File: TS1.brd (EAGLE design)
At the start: 32 x 22 mm, 20 parts, among them IC1 AT42QT1010, J1 PWR, Q1 2N7002

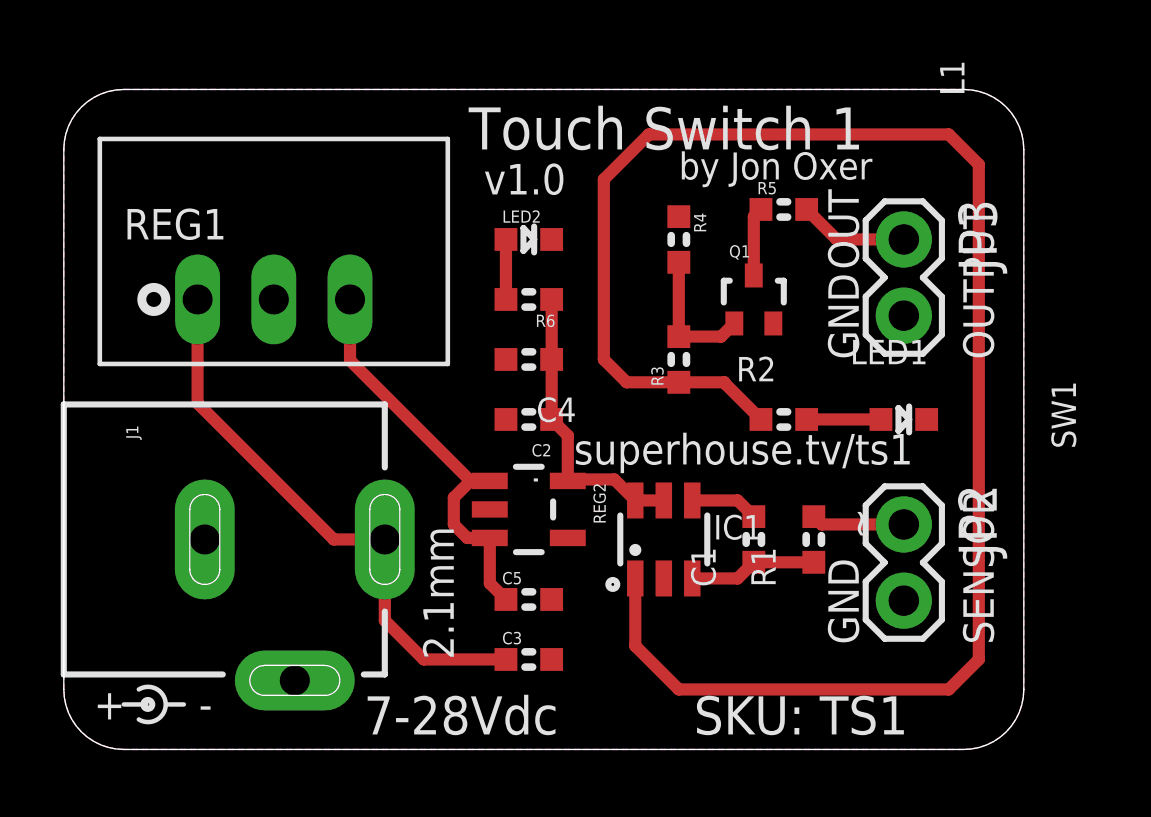
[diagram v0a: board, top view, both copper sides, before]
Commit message: Added mounting hole
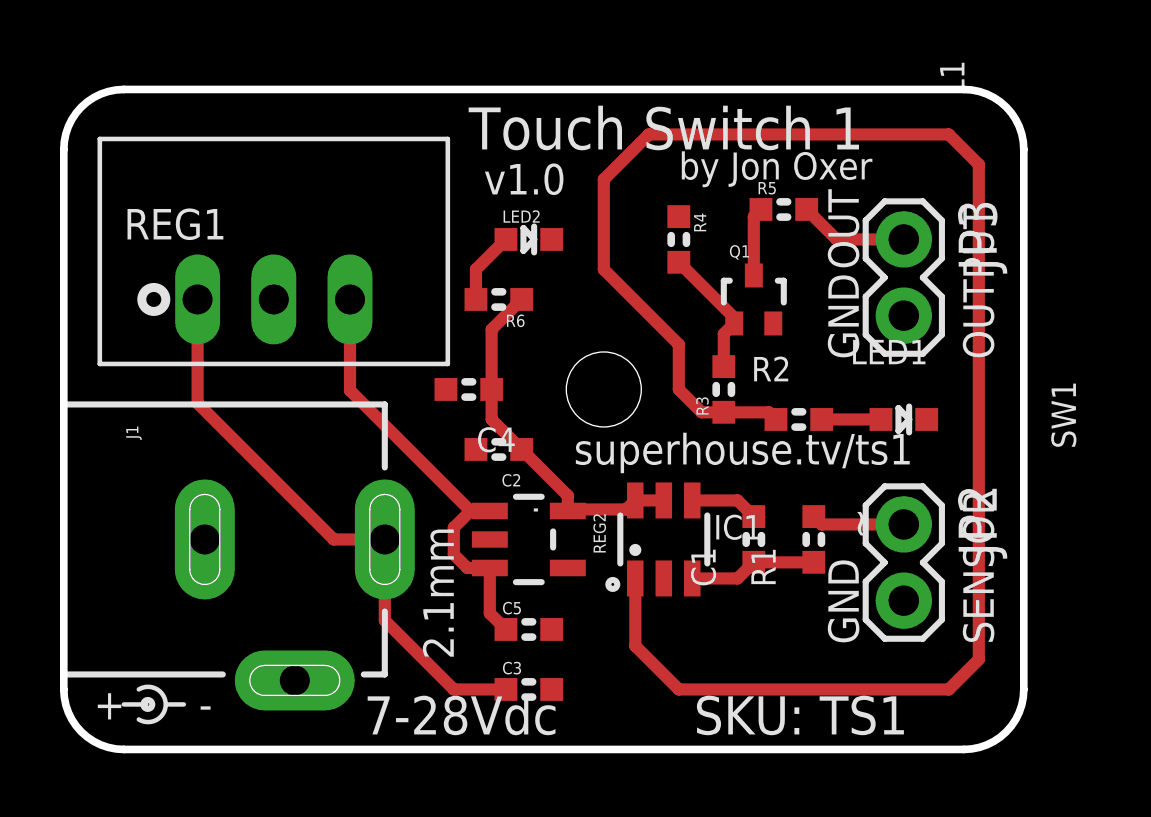
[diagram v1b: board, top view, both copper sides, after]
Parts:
- moved C4 2.24 mm to (13.5, 12.0)
- moved R3 1.80 mm to (22.0, 12.0)
- moved C2 1.41 mm to (14.5, 10.0)
- moved C3 1.00 mm to (15.5, 2.00)
- moved C5 1.00 mm to (15.5, 4.00)
- moved R6 1.00 mm to (14.5, 15.0)
- moved REG2 1.00 mm to (15.5, 7.00)
- moved R2 0.50 mm to (24.5, 11.0)
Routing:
- net VDD: track 9.78 -> 11.9 mm
- net N$8: track 13.7 -> 14.7 mm
- net N$6: track 2.48 -> 1.98 mm
